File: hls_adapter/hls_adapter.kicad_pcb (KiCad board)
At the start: 2 copper layers, 43 x 21 mm, 11 parts, among them J1 JST PH2.0 B4B Vert, J2 JST PH2.0 B2B Vert, J3 JST PH B4B Vert, J4 JST PH2.0 B5B Vert, Q1 AS2302, U1 DNP LM2596

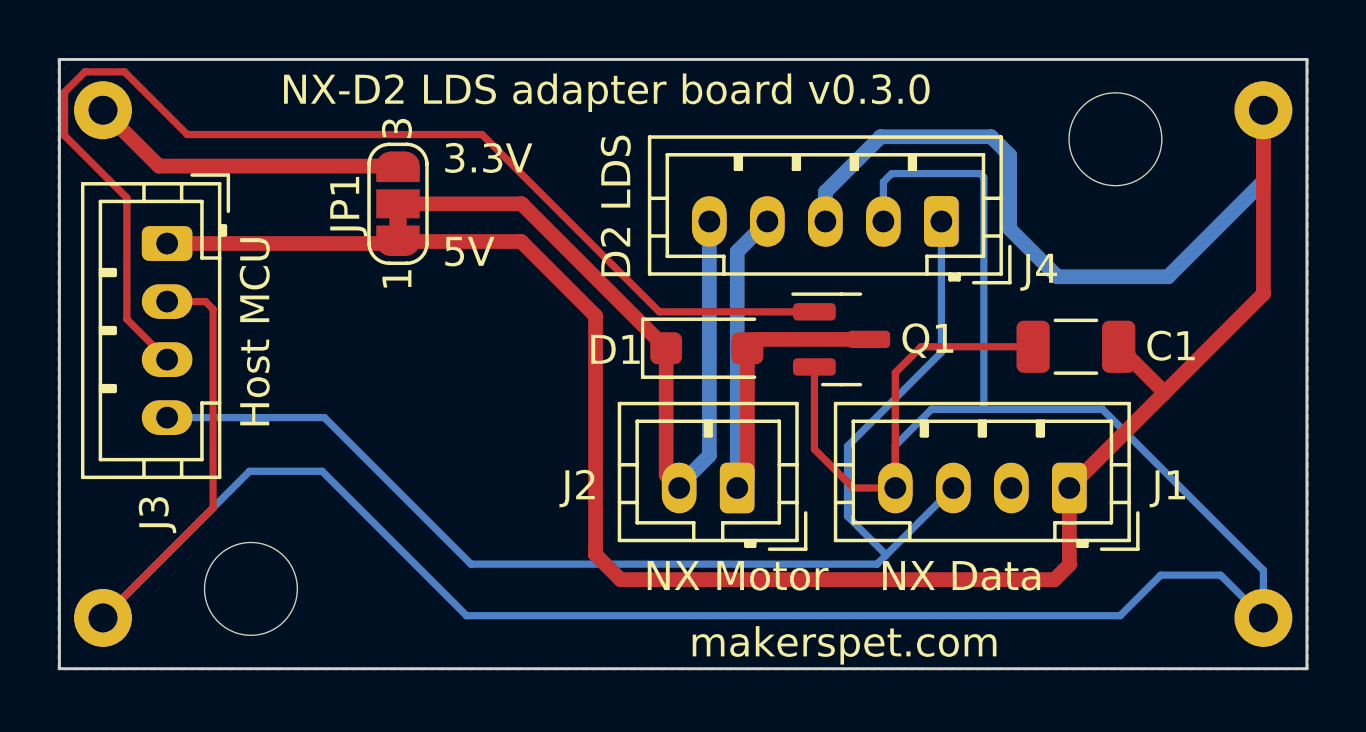
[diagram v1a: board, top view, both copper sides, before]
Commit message: HLS Adapter done
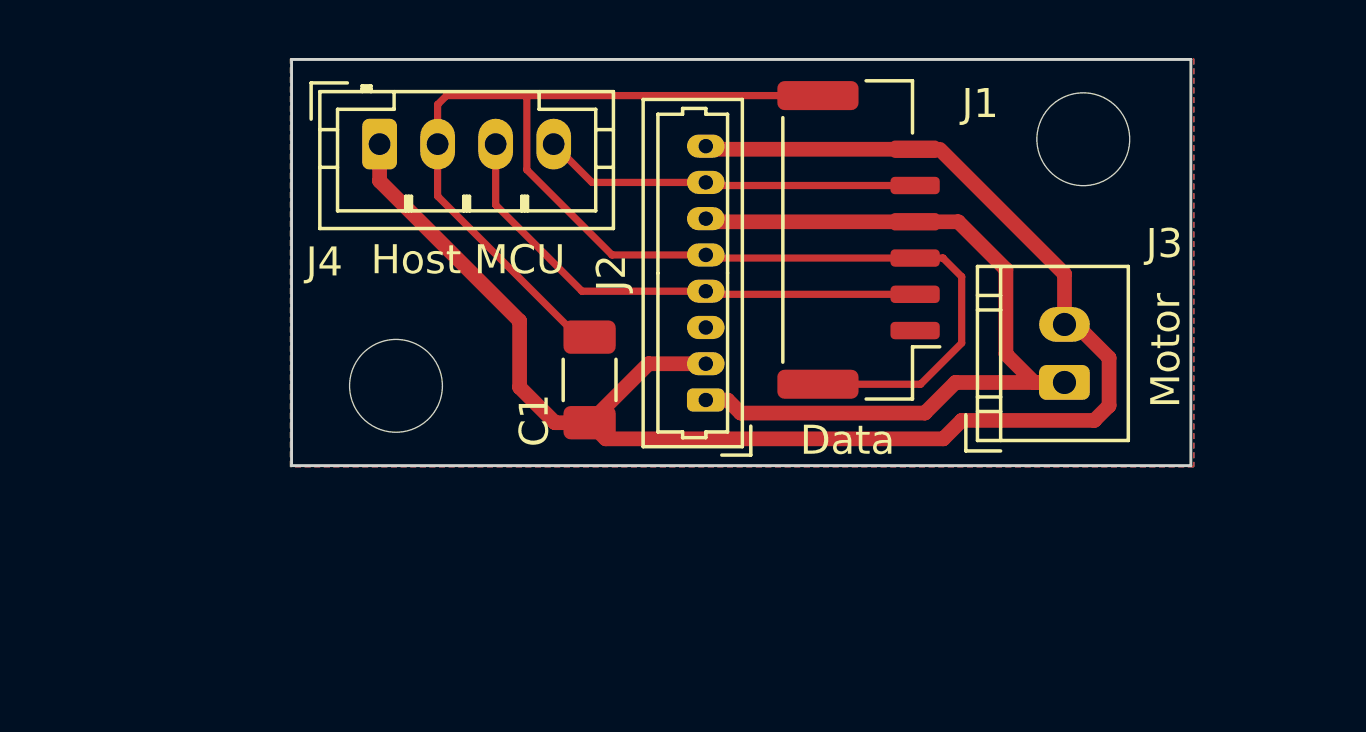
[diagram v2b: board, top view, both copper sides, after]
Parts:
- removed D1: FS26, Diode_SMD:D_SOD-123F
- removed JP1: SolderJumper_3_Bridged12, Jumper:SolderJumper-3_P1.3mm_Bridged12_RoundedPad1.0x1.5mm_NumberLabels
- removed Q1: AS2302, Package_TO_SOT_SMD:SOT-23
- removed U1: DNP LM2596, Makerspet:LM2596 Module
- J1: value JST PH2.0 B4B Vert -> JST GH 1.25 6P SKT VERT SMD; footprint Connector_JST:JST_PH_B4B-PH-K_1x04_P2.00mm_Vertical -> Connector_JST:JST_GH_BM06B-GHS-TBT_1x06-1MP_P1.25mm_Vertical
- J2: value JST PH2.0 B2B Vert -> Molex PicoBlade 1.25 8P SKT VERT; footprint Connector_JST:JST_PH_B2B-PH-K_1x02_P2.00mm_Vertical -> Makerspet:Molex_PicoBlade_53047-0810_1x08_P1.25mm_Vertical
- J3: value JST PH B4B Vert -> SMW200-H02G 2.0 2P SKT VERT; footprint Connector_JST:JST_PH_B4B-PH-K_1x04_P2.00mm_Vertical -> Makerspet:SMW200_02
- J4: value JST PH2.0 B5B Vert -> JST PH B4B SKT VERT SMD; footprint Connector_JST:JST_PH_B5B-PH-K_1x05_P2.00mm_Vertical -> Connector_JST:JST_PH_B4B-PH-K_1x04_P2.00mm_Vertical
- moved J3 31.3 mm to (113.1, 50.6), turned to 90 degrees
- moved J4 19.5 mm to (89.5, 42.4), turned to 0 degrees
- moved C1 16.8 mm to (96.8, 50.5), turned to 90 degrees
- moved J1 11.2 mm to (106.0, 45.7), turned to 90 degrees
- moved H1 8.60 mm to (90.1, 50.8)
- moved J2 3.22 mm to (100.8, 51.2), turned to 90 degrees
- moved H2 1.11 mm to (113.8, 42.2)
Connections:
- J1 pad 1: +5V -> unconnected-(J1-Pin_1-Pad1)
- J1 pad 2: unconnected-(J1-Pin_2-Pad2) -> /RX
- J1 pad 3: /TX -> GND
- J1 pad 4: GND -> /MOT-
- J2 pad 2: /MOT+ -> +5V
- J3 pad 1: +5V -> /MOT-
- J3 pad 2: GND -> +5V
- J4 pad 1: /TX -> +5V
- J4 pad 3: +5V -> /RX
- J4 pad 4: /MOT- -> /TX
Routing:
- net GND: track 106.1 -> 50.7 mm
- net /MOT_EN: track 40.2 -> 0.00 mm
- net /TX: track 43.7 -> 13.1 mm
- net +5V: track 85.9 -> 56.4 mm
- net /MOT+: track 25.9 -> 0.00 mm
- net /RX: track 0.00 -> 17.8 mm
- net +3.3V: track 11.0 -> 0.00 mm
- net /MOT-: track 18.9 -> 29.4 mm
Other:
- board size 43 x 21 mm -> 31 x 14 mm
- board text added: "Data"
- board text added: "HLS Adapter Board v0.1.0"
- board text added: "Motor"
- board text removed: "3.3V 5V"
- board text removed: "D2 LDS"
- board text removed: "NX Motor NX Data"
- board text removed: "NX-D2 LDS adapter board v0.3.0"

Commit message: ZH extension connector; 6-pin LDS connector
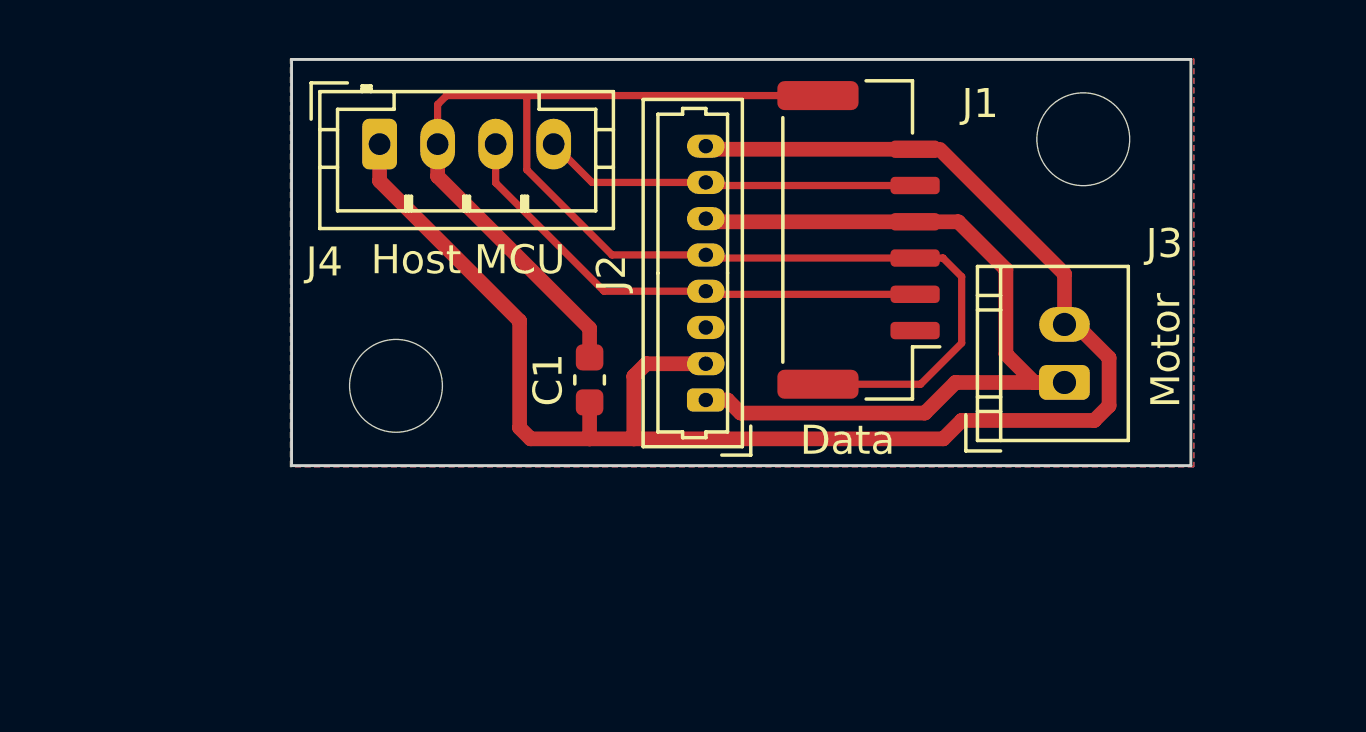
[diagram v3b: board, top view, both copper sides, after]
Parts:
- C1: value 100uF -> 22uF; footprint Capacitor_SMD:C_1206_3216Metric -> Capacitor_SMD:C_0603_1608Metric
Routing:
- net +5V: track 56.4 -> 58.4 mm
